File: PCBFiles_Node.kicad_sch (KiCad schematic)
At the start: 15 parts, among them IC1 STM32L432KCU3, U1 RFM9X, U2 XC6206P332MR, Y1 Crystal_Small

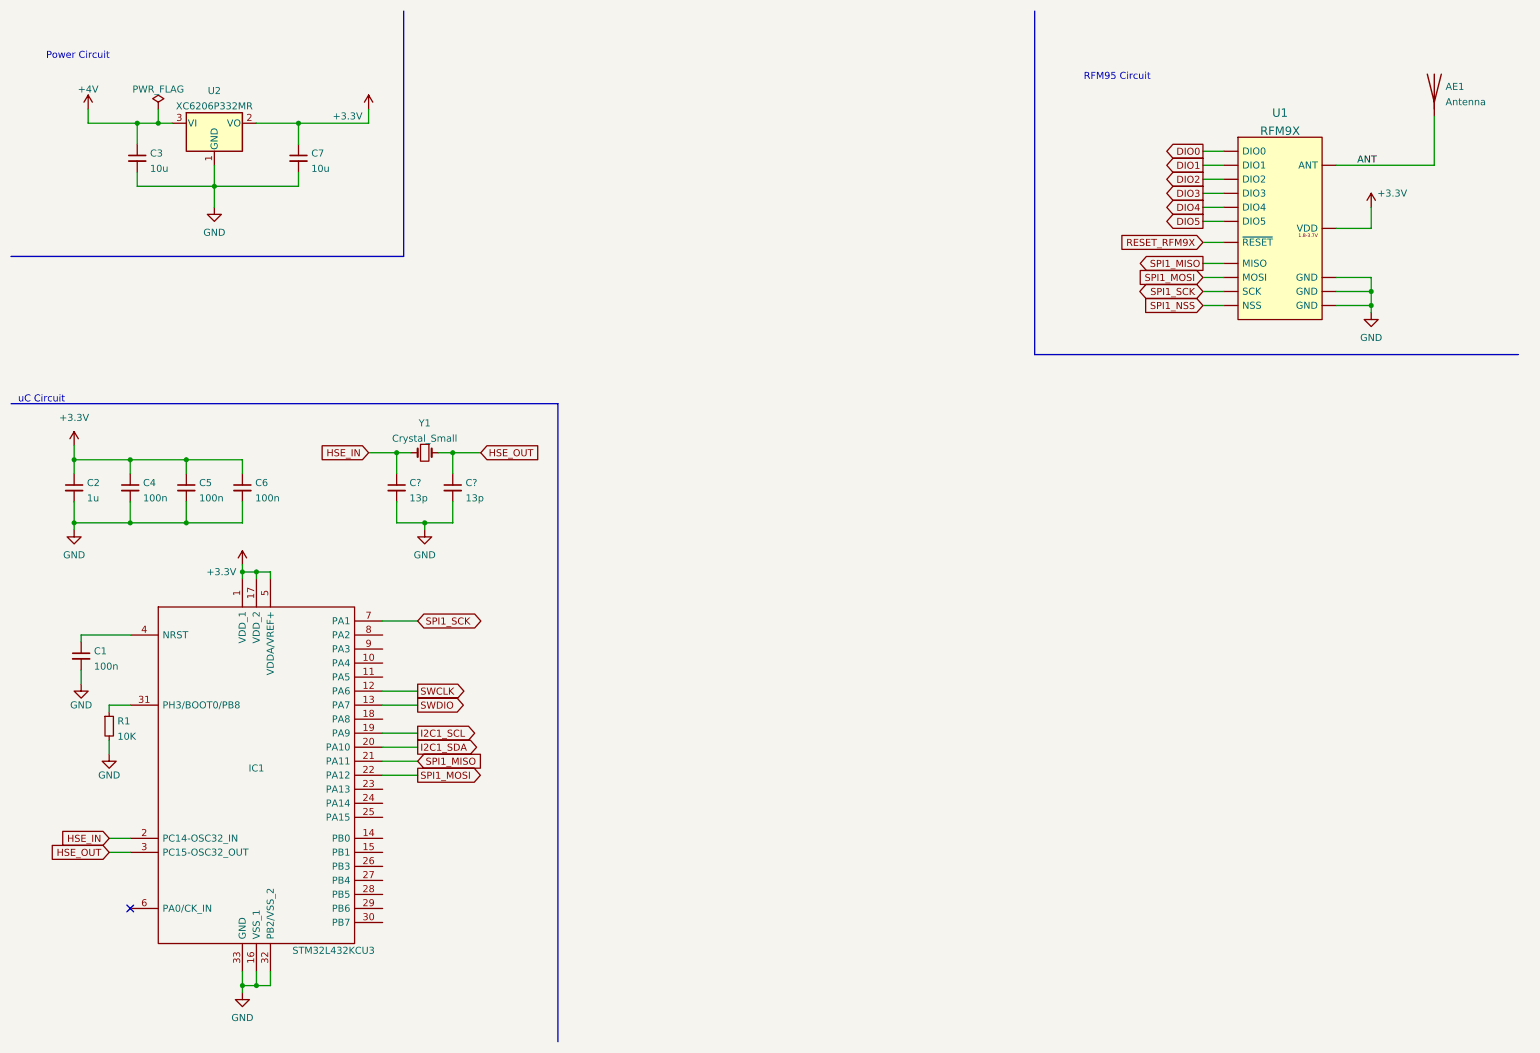
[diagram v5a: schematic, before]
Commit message: Connectors, MPU Circuit & Pins Schematic Update
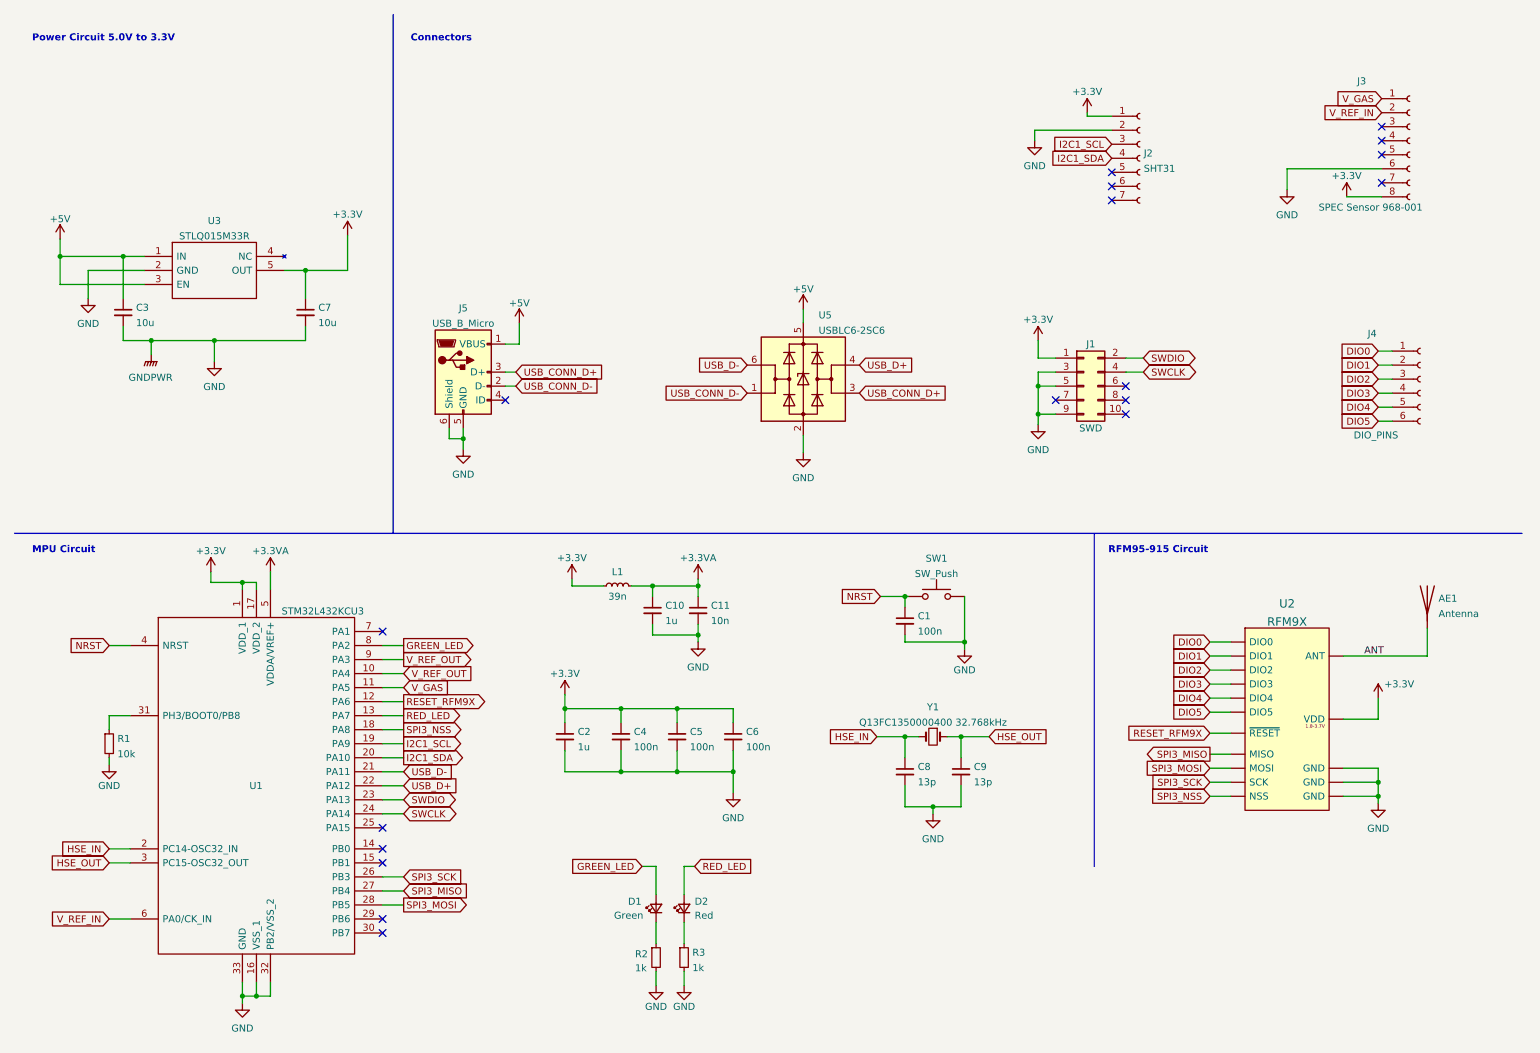
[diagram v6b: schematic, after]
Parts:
- removed U2: XC6206P332MR, Package_TO_SOT_SMD:SOT-23, symbol Regulator_Linear:XC6206PxxxMR
- added C10: 1u, symbol Device:C_Small
- added C11: 10n, symbol Device:C_Small
- added D1: Green, symbol Device:LED_Small
- added D2: Red, symbol Device:LED_Small
- added J1: SWD, symbol Connector_Generic:Conn_02x05_Odd_Even
- added J2: SHT31, symbol Connector:Conn_01x07_Female
- added J3: SPEC Sensor 968-001, symbol Connector:Conn_01x08_Female
- added J4: DIO_PINS, symbol Connector:Conn_01x06_Female
- added J5: USB_B_Micro, symbol Connector:USB_B_Micro
- added L1: 39n, symbol Device:L_Small
- added R2, R3: 1k, symbol Device:R_Small
- added SW1: SW_Push, symbol Switch:SW_Push
- added U3: STLQ015M33R, SamacSys_Parts:SOT95P280X145-5N, symbol SamacSys_Parts:STLQ015M33R
- added U5: USBLC6-2SC6, Package_TO_SOT_SMD:SOT-23-6, symbol Power_Protection:USBLC6-2SC6
- R1: value 10K -> 10k
- Y1: value Crystal_Small -> Q13FC1350000400 32.768kHz; footprint (none) -> Crystal:Q13FC1350000400
- gave numbers to parts that had none: 2
- renumbered IC1 to U1, U1 to U2
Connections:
- net SPI1_NSS is gone; now on net SPI3_NSS: U2.5 (NSS)
- net +3V3: now also J1.1 (Pin_1), J2.1 (Pin_1), J3.8 (Pin_8), L1.1, U3.5 (OUT); no longer U1.5 (VDDA/VREF+)
- net DIO0: now also J4.1 (Pin_1)
- net DIO1: now also J4.2 (Pin_2)
- net DIO2: now also J4.3 (Pin_3)
- net DIO3: now also J4.4 (Pin_4)
- net DIO4: now also J4.5 (Pin_5)
- net DIO5: now also J4.6 (Pin_6)
- net GND: now also C10.2, C11.2, J1.3 (Pin_3), J1.5 (Pin_5), J1.9 (Pin_9), J2.2 (Pin_2), J3.6 (Pin_6), J5.5 (GND), J5.6 (Shield), R2.2, R3.2, SW1.2, U3.2 (GND), U5.2 (GND)
- net I2C1_SCL: now also J2.3 (Pin_3)
- net I2C1_SDA: now also J2.4 (Pin_4)
- net RESET_RFM9X: now also U1.12 (PA6)
- net SWCLK: now also U1.24 (PA14), J1.4 (Pin_4); no longer U1.12 (PA6)
- net SWDIO: now also U1.23 (PA13), J1.2 (Pin_2); no longer U1.13 (PA7)
- net V_REF_OUT: now reaches U1.10 (PA4)
- net V_REF_OUT: now also U1.9 (PA3)
- net V_GAS: now reaches U1.11 (PA5)
- net V_GAS: now also J3.1 (Pin_1)
- net SPI3_NSS: now reaches U1.18 (PA8)
- net SPI3_SCK: now reaches U1.26 (PB3)
- net SPI3_SCK: now also U2.4 (SCK)
- net SPI3_MISO: now reaches U1.27 (PB4)
- net SPI3_MISO: now also U2.2 (MISO)
- net SPI3_MOSI: now reaches U1.28 (PB5)
- net SPI3_MOSI: now also U2.3 (MOSI)
- net NRST: now reaches C1.1, U1.4 (NRST)
- net NRST: now also SW1.1
- net V_REF_IN: now reaches U1.6 (PA0/CK_IN)
- net V_REF_IN: now also J3.2 (Pin_2)
- net GREEN_LED: now reaches U1.8 (PA2)
- net GREEN_LED: now also D1.2 (A)
- net +4V renamed +5V
- net +5V: now also J5.1 (VBUS), U3.1 (IN), U3.3 (EN), U5.5 (VBUS)
- net SPI1_MISO renamed USB_D-
- net USB_D-: now also U5.6 (I/O1); no longer U2.2 (MISO)
- net SPI1_MOSI renamed USB_D+
- net USB_D+: now also U5.4 (I/O2); no longer U2.3 (MOSI)
- net SPI1_SCK: no longer names the net of U1.7 (PA1)
- net SPI1_SCK: no longer U2.4 (SCK)
- new net: D1.1 (K), R2.1
- new net: D2.1 (K), R3.1
- new net +3.3VA: C10.1, C11.1, L1.2, U1.5 (VDDA/VREF+)
- new net RED_LED: D2.2 (A), U1.13 (PA7)
- new net USB_CONN_D+: J5.3 (D+), U5.3 (I/O2)
- new net USB_CONN_D-: J5.2 (D-), U5.1 (I/O1)
- no-connect marks 1 -> 18
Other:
- note added: "Connectors"
- note added: "MPU Circuit"
- note added: "Power Circuit 5.0V to 3.3V"
- note added: "RFM95-915 Circuit"
- note removed: "Power Circuit"
- note removed: "RFM95 Circuit"
- note removed: "uC Circuit"
- moved on the sheet: AE1, C2, C4, C5, C6, C8, C9, R1, U1, U2, Y1

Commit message: First PCB Design
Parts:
- removed AE1: Antenna, symbol Device:Antenna
- removed J3: SPEC Sensor 968-001, symbol Connector:Conn_01x08_Female
- removed J4: DIO_PINS, symbol Connector:Conn_01x06_Female
- added H1, H2: MountingHole, MountingHole:MountingHole_2.2mm_M2_Pad_Via, symbol Mechanical:MountingHole
- added J3: SPEC Sensor 968-001, Connector_PinHeader_2.54mm:PinHeader_1x08_P2.54mm_Horizontal, symbol Connector:Conn_01x08_Male
- added J6: Input, TerminalBlock:TerminalBlock_bornier-2_P5.08mm, symbol Connector:Screw_Terminal_01x02
- added J7: SMA, Connector_Coaxial:SMA_Samtec_SMA-J-P-X-ST-EM1_EdgeMount, symbol Connector:Conn_Coaxial
- C1, C10, C11, C2, C4, C5, C6, C8, C9: footprint (none) -> Capacitor_SMD:C_0402_1005Metric
- C3, C7: footprint (none) -> Capacitor_SMD:C_1206_3216Metric
- D1, D2: footprint (none) -> LED_SMD:LED_0201_0603Metric
- J1: footprint (none) -> Connector_PinHeader_2.54mm:PinHeader_2x05_P2.54mm_Vertical_SMD
- J2: footprint (none) -> Connector_PinSocket_2.54mm:PinSocket_1x07_P2.54mm_Vertical
- J5: footprint (none) -> Connector_USB:USB_Micro-B_Molex-105017-0001
- L1: footprint (none) -> Inductor_SMD:L_0402_1005Metric
- R1: footprint (none) -> Resistor_SMD:R_0402_1005Metric
- R2, R3: footprint (none) -> Resistor_SMD:R_0603_1608Metric
- SW1: footprint (none) -> Button_Switch_SMD:SW_SPST_B3U-1000P
- U1: value STM32L432KCU3 -> STM32L432KCUx
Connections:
- net +3V3: now also J3.8 (Pin_8)
- net +5V: now also J6.1 (Pin_1)
- net ANT: now also J7.1 (In)
- net GND: now also J3.6 (Pin_6), J6.2 (Pin_2), J7.2 (Ext)
- net V_GAS: now also J3.1 (Pin_1)
- net V_REF_IN: now also J3.2 (Pin_2)
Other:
- moved on the sheet: C1, SW1

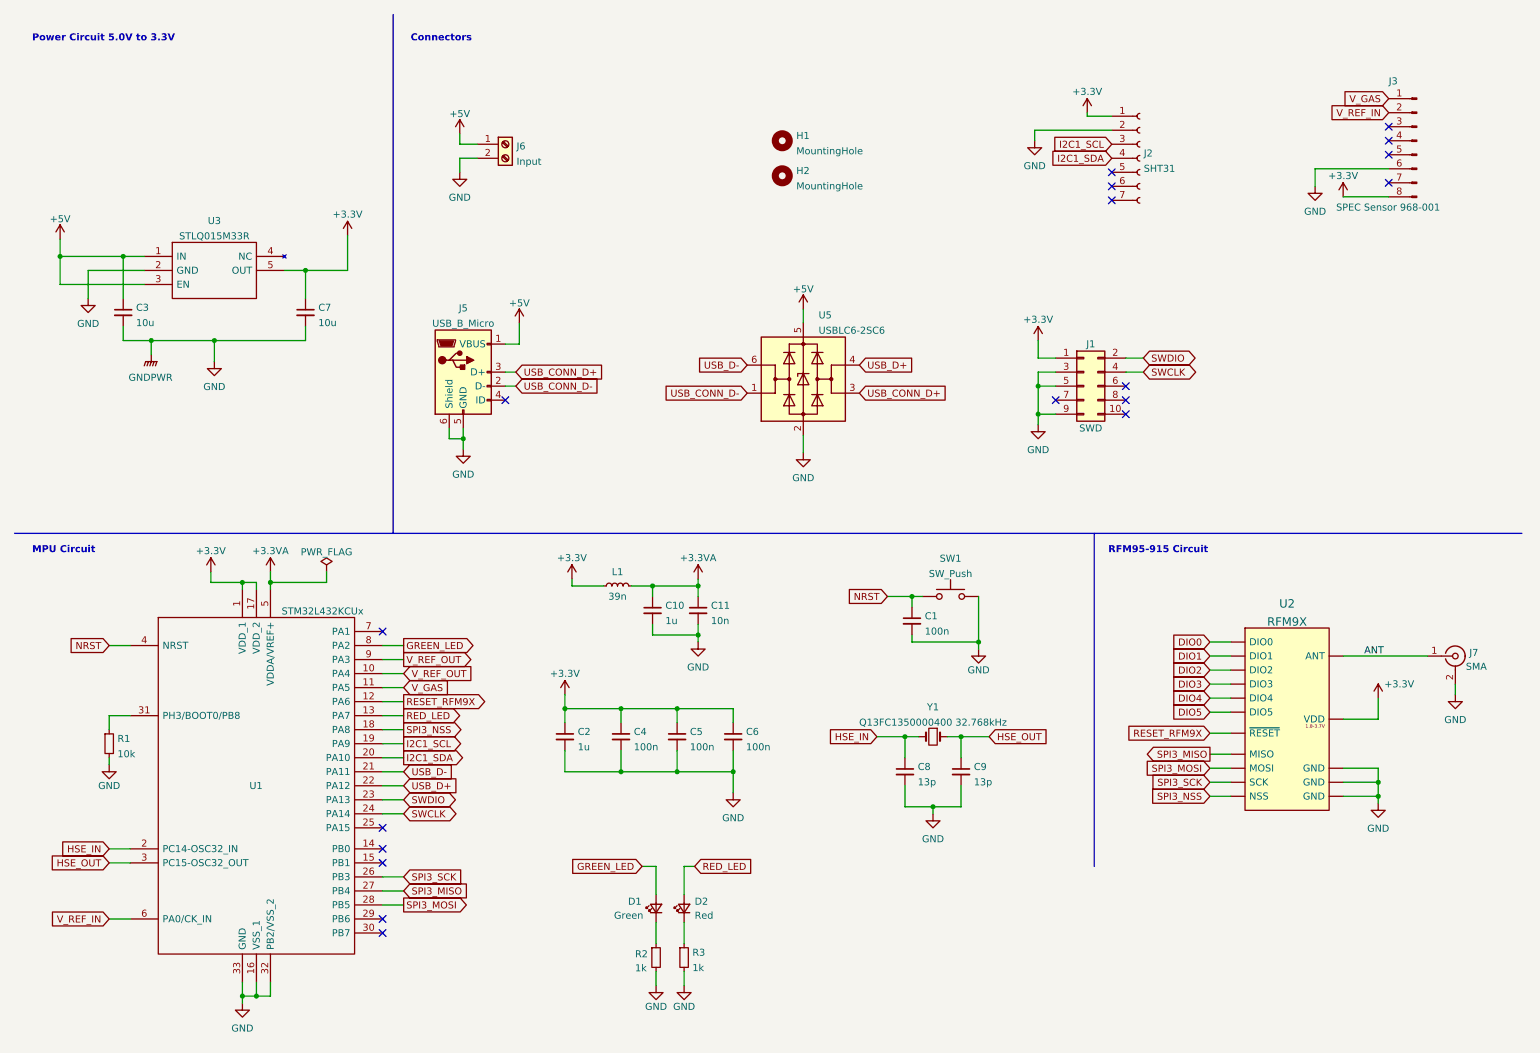
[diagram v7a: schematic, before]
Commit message: Replaced STM32L432KCU6 for STM32L431RCTx in Schematic and PCB
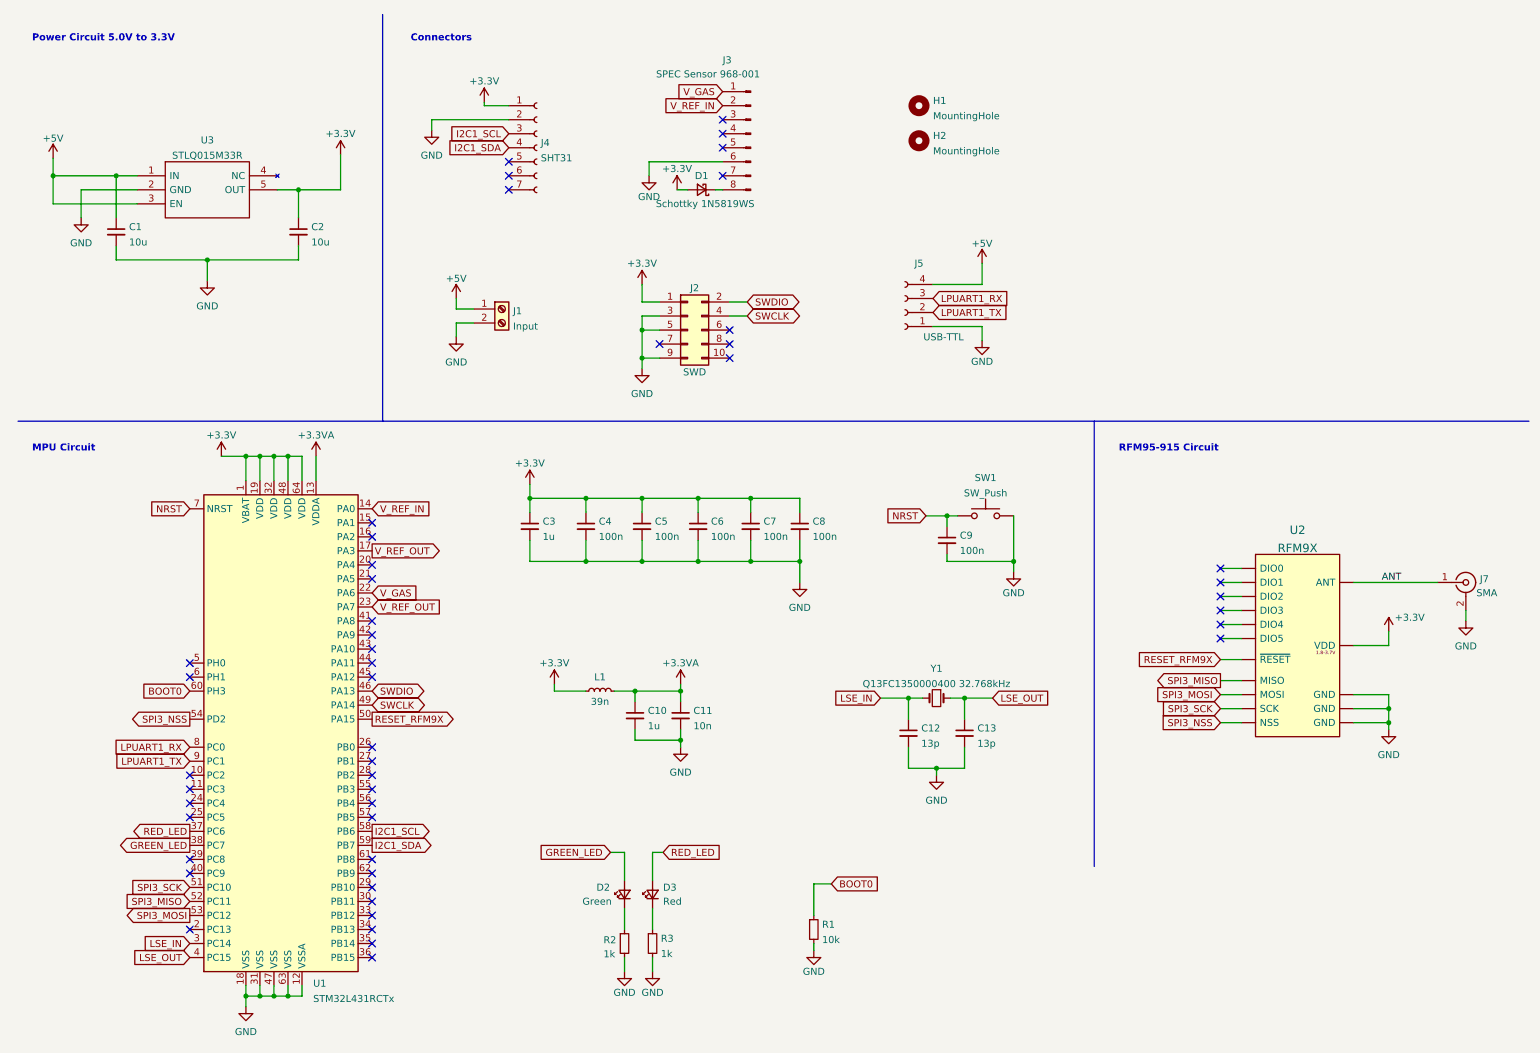
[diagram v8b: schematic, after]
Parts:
- removed J5: USB_B_Micro, Connector_USB:USB_Micro-B_Molex-105017-0001, symbol Connector:USB_B_Micro
- removed U1: STM32L432KCUx, SamacSys_Parts:QFN50P500X500X60-33N-D, symbol SamacSys_Parts:STM32L432KCU3
- removed U5: USBLC6-2SC6, Package_TO_SOT_SMD:SOT-23-6, symbol Power_Protection:USBLC6-2SC6
- added C7, C8: 100n, Capacitor_SMD:C_0402_1005Metric, symbol Device:C_Small
- added D1: Schottky 1N5819WS, Diode_SMD:D_SOD-323, symbol Device:D_Schottky_Small
- added J5: USB-TTL, Connector_PinSocket_2.54mm:PinSocket_1x04_P2.54mm_Horizontal, symbol Connector:Conn_01x04_Female
- added U1: STM32L431RCTx, Package_QFP:LQFP-64_10x10mm_P0.5mm, symbol MCU_ST_STM32L4:STM32L431RCTx
- renumbered C3 to C1, C8 to C12, C9 to C13, C7 to C2, C2 to C3, C1 to C9, D1 to D2, D2 to D3, J6 to J1, J1 to J2, J2 to J4
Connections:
- net +3.3VA: now also U1.13 (VDDA)
- net +3V3: now also C7.1, C8.1, D1.2 (A), U1.1 (VBAT), U1.19 (VDD), U1.32 (VDD), U1.48 (VDD), U1.64 (VDD); no longer J3.8 (Pin_8)
- net +5V: now also J5.4 (Pin_4)
- net GND: now also C7.2, C8.2, J5.1 (Pin_1), U1.12 (VSSA), U1.18 (VSS), U1.31 (VSS), U1.47 (VSS), U1.63 (VSS)
- net GREEN_LED: now also U1.38 (PC7)
- net I2C1_SCL: now also U1.58 (PB6)
- net I2C1_SDA: now also U1.59 (PB7)
- net NRST: now also U1.7 (NRST)
- net RED_LED: now also U1.37 (PC6)
- net RESET_RFM9X: now also U1.50 (PA15)
- net SPI3_MISO: now also U1.52 (PC11)
- net SPI3_MOSI: now also U1.53 (PC12)
- net SPI3_NSS: now also U1.54 (PD2)
- net SPI3_SCK: now also U1.51 (PC10)
- net SWCLK: now also U1.49 (PA14)
- net SWDIO: now also U1.46 (PA13)
- net V_GAS: now also U1.22 (PA6)
- net V_REF_IN: now also U1.14 (PA0)
- net V_REF_OUT: now also U1.17 (PA3), U1.23 (PA7)
- net BOOT0: now reaches R1.1
- net BOOT0: now also U1.60 (PH3)
- net DIO0: no longer names the net of U2.11 (DIO0)
- net DIO1: no longer names the net of U2.10 (DIO1)
- net DIO2: no longer names the net of U2.9 (DIO2)
- net DIO3: no longer names the net of U2.14 (DIO3)
- net DIO4: no longer names the net of U2.13 (DIO4)
- net DIO5: no longer names the net of U2.7 (DIO5)
- net HSE_IN renamed LSE_IN
- net LSE_IN: now also U1.3 (PC14)
- net HSE_OUT renamed LSE_OUT
- net LSE_OUT: now also U1.4 (PC15)
- new net: D1.1 (K), J3.8 (Pin_8)
- new net LPUART1_RX: J5.3 (Pin_3), U1.8 (PC0)
- new net LPUART1_TX: J5.2 (Pin_2), U1.9 (PC1)
- no-connect marks 18 -> 49
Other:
- moved on the sheet: C1, C10, C11, C12, C13, C2, C3, C4, C5, C6, C9, D2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
